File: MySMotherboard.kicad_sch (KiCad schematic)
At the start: 52 parts, among them SW1 RST, SW2 BTN, U1 MCP1640Cx-xCHY, U2 APE8865Y5-30-HF-3, U3 ATmega328PB-A, U4 AT25xxx, U5 RFM69HW, U6 ATSHA204A, U7 AP63205WU, U8 SP3481EN, X2 MySX 2.5, X3 ANT, Y1 16M

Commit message: add reverse polarity protection for 24V input
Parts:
- added Q2: ~, Package_TO_SOT_SMD:SOT-23, symbol Device:Q_PMOS_GSD
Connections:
- net +24V: now also Q2.2 (S); no longer X4.1 (Pin_1)
- net GND: now also Q2.1 (G)
- net SW_L2: no longer names the net of C6.2, L2.1, U7.5 (SW)
- new net: Q2.3 (D), X4.1 (Pin_1)
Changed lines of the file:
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@@
   (junction (at 57.15 78.105) (diameter 0) (color 0 0 0 0)
   )
+  (junction (at 254 121.285) (diameter 0) (color 0 0 0 0)
+  )
   (junction (at 63.5 31.115) (diameter 0) (color 0 0 0 0)
   )
@@
   (junction (at 82.55 90.17) (diameter 0) (color 0 0 0 0)
   )
-  (junction (at 271.78 130.81) (diameter 0) (color 0 0 0 0)
-  )
   (no_connect (at 180.975 144.78))
   (no_connect (at 180.975 139.7))
@@
     (stroke (width 0) (type default))
   )
+  (wire (pts (xy 264.16 121.285) (xy 271.78 121.285))
+    (stroke (width 0) (type default))
+  )
   (wire (pts (xy 72.39 121.285) (xy 111.125 121.285))
     (stroke (width 0.1524) (type solid))
@@
     (stroke (width 0.1524) (type solid))
   )
-  (wire (pts (xy 271.78 129.54) (xy 271.78 130.81))
-    (stroke (width 0) (type default))
-  )
   (wire (pts (xy 37.465 31.115) (xy 41.91 31.115))
     (stroke (width 0.1524) (type solid))
@@
     (stroke (width 0.1524) (type solid))
   )
-  (wire (pts (xy 271.78 130.81) (xy 271.78 134.62))
-    (stroke (width 0) (type default))
-  )
   (wire (pts (xy 195.58 41.275) (xy 200.025 41.275))
     (stroke (width 0.1524) (type solid))
@@
     (stroke (width 0) (type default))
   )
-  (wire (pts (xy 267.97 128.27) (xy 267.97 130.81))
-    (stroke (width 0) (type default))
-  )
   (wire (pts (xy 238.76 44.45) (xy 252.095 44.45))
     (stroke (width 0) (type default))
@@
     (stroke (width 0) (type default))
   )
+  (wire (pts (xy 251.46 121.285) (xy 254 121.285))
+    (stroke (width 0) (type default))
+  )
   (wire (pts (xy 182.245 41.275) (xy 195.58 41.275))
     (stroke (width 0.1524) (type solid))
@@
     (stroke (width 0.1524) (type solid))
   )
-  (wire (pts (xy 271.78 130.81) (xy 267.97 130.81))
-    (stroke (width 0) (type default))
-  )
   (wire (pts (xy 262.255 24.765) (xy 262.255 31.115))
     (stroke (width 0) (type default))
@@
     (stroke (width 0.1524) (type solid))
   )
+  (wire (pts (xy 271.78 121.285) (xy 271.78 134.62))
+    (stroke (width 0) (type default))
+  )
   (wire (pts (xy 55.88 31.115) (xy 63.5 31.115))
     (stroke (width 0) (type default))
@@
     (effects (font (size 1.27 1.27)) (justify left bottom))
   )
-  (label "SW_L2" (at 264.795 24.765 180) (fields_autoplaced)
-    (effects (font (size 1.27 1.27)) (justify right bottom))
-  )
   (label "A5" (at 78.105 121.285 0) (fields_autoplaced)
     (effects (font (size 1.2446 1.2446)) (justify left bottom))
@@
     )
   )
+  (netclass_flag "" (length 2.54) (shape round) (at 265.43 121.285 0) (fields_autoplaced)
+    (effects (font (size 1.27 1.27)) (justify left bottom))
+    (property "Netclass" "Power" (at 266.1285 118.745 0)
+      (effects (font (size 1.27 1.27) italic) (justify left))
+    )
+  )
+  (netclass_flag "" (length 2.54) (shape round) (at 262.255 24.765 0) (fields_autoplaced)
+    (effects (font (size 1.27 1.27)) (justify left bottom))
+    (property "Netclass" "Power" (at 261.5565 22.225 0)
+      (effects (font (size 1.27 1.27) italic) (justify right))
+    )
+  )
   (symbol (lib_id "power:GND") (at 88.9 81.28 0) (mirror x) (unit 1)
     (in_bom yes) (on_board yes) (dnp no) (fields_autoplaced)
@@
     )
   )
-  (symbol (lib_id "power:+24V") (at 267.97 128.27 0) (unit 1)
-    (in_bom yes) (on_board yes) (dnp no) (fields_autoplaced)
-    (property "Reference" "#PWR026" (at 267.97 132.08 0)
+  (symbol (lib_id "power:+24V") (at 254 121.285 0) (unit 1)
+    (in_bom yes) (on_board yes) (dnp no)
+    (property "Reference" "#PWR026" (at 254 125.095 0)
       (effects (font (size 1.27 1.27)) hide)
     )
-    (property "Value" "+24V" (at 267.97 123.19 0)
+    (property "Value" "+24V" (at 254 116.84 0)
       (effects (font (size 1.27 1.27)))
     )
-    (property "Footprint" "" (at 267.97 128.27 0)
+    (property "Footprint" "" (at 254 121.285 0)
       (effects (font (size 1.27 1.27)) hide)
     )
-    (property "Datasheet" "" (at 267.97 128.27 0)
+    (property "Datasheet" "" (at 254 121.285 0)
       (effects (font (size 1.27 1.27)) hide)
     )
@@
     )
   )
+  (symbol (lib_id "power:PWR_FLAG") (at 251.46 121.285 0) (mirror y) (unit 1)
+    (in_bom yes) (on_board yes) (dnp no)
+    (property "Reference" "#FLG04" (at 251.46 119.38 0)
+      (effects (font (size 1.27 1.27)) hide)
+    )
+    (property "Value" "PWR_FLAG" (at 250.825 117.475 0)
+      (effects (font (size 1.27 1.27)) (justify left))
+    )
+    (property "Footprint" "" (at 251.46 121.285 0)
+      (effects (font (size 1.27 1.27)) hide)
+    )
+    (property "Datasheet" "~" (at 251.46 121.285 0)
+      (effects (font (size 1.27 1.27)) hide)
+    )
+    (pin "1")
+    (instances
+      (project "MySMotherboard"
+        (path "/005ccf98-7ec2-4789-9497-178572c51999"
+          (reference "#FLG04") (unit 1)
+        )
+      )
+    )
+  )
   (symbol (lib_id "power:GND") (at 57.15 154.305 0) (unit 1)
     (in_bom yes) (on_board yes) (dnp no) (fields_autoplaced)
@@
     )
   )
-  (symbol (lib_id "power:PWR_FLAG") (at 271.78 129.54 0) (unit 1)
-    (in_bom yes) (on_board yes) (dnp no)
-    (property "Reference" "#FLG04" (at 271.78 127.635 0)
-      (effects (font (size 1.27 1.27)) hide)
-    )
-    (property "Value" "PWR_FLAG" (at 271.78 124.46 0)
-      (effects (font (size 1.27 1.27)) (justify left))
-    )
-    (property "Footprint" "" (at 271.78 129.54 0)
-      (effects (font (size 1.27 1.27)) hide)
-    )
-    (property "Datasheet" "~" (at 271.78 129.54 0)
-      (effects (font (size 1.27 1.27)) hide)
-    )
-    (pin "1")
-    (instances
-      (project "MySMotherboard"
-        (path "/005ccf98-7ec2-4789-9497-178572c51999"
-          (reference "#FLG04") (unit 1)
-        )
-      )
-    )
-  )
   (symbol (lib_id "Device:C") (at 58.42 47.625 0) (mirror y) (unit 1)
     (in_bom yes) (on_board yes) (dnp no)
@@
     )
   )
+  (symbol (lib_id "power:GND") (at 259.08 128.905 0) (unit 1)
+    (in_bom yes) (on_board yes) (dnp no) (fields_autoplaced)
+    (property "Reference" "#PWR025" (at 259.08 135.255 0)
+      (effects (font (size 1.27 1.27)) hide)
+    )
+    (property "Value" "GND" (at 259.08 133.35 0)
+      (effects (font (size 1.27 1.27)))
+    )
+    (property "Footprint" "" (at 259.08 128.905 0)
+      (effects (font (size 1.27 1.27)) hide)
+    )
+    (property "Datasheet" "" (at 259.08 128.905 0)
+      (effects (font (size 1.27 1.27)) hide)
+    )
+    (pin "1")
+    (instances
+      (project "MySMotherboard"
+        (path "/005ccf98-7ec2-4789-9497-178572c51999"
+          (reference "#PWR025") (unit 1)
+        )
+      )
+    )
+  )
   (symbol (lib_id "power:PWR_FLAG") (at 55.88 31.115 180) (unit 1)
     (in_bom yes) (on_board yes) (dnp no) (fields_autoplaced)
@@
         )
       )
+    )
+  )
+  (symbol (lib_id "Device:Q_PMOS_GSD") (at 259.08 123.825 270) (mirror x) (unit 1)
+    (in_bom yes) (on_board yes) (dnp no)
+    (property "Reference" "Q2" (at 259.08 116.84 90)
+      (effects (font (size 1.27 1.27)))
+    )
+    (property "Value" "~" (at 259.08 116.84 90)
+      (effects (font (size 1.27 1.27)))
+    )
+    (property "Footprint" "Package_TO_SOT_SMD:SOT-23" (at 261.62 118.745 0)
+      (effects (font (size 1.27 1.27)) hide)
+    )
+    (property "Datasheet" "~" (at 259.08 123.825 0)
+      (effects (font (size 1.27 1.27)) hide)
+    )
+    (pin "2")
+    (pin "1")
+    (pin "3")
+    (instances
+      (project "MySMotherboard"
+        (path "/005ccf98-7ec2-4789-9497-178572c51999"
+          (reference "Q2") (unit 1)
+        )
+      )

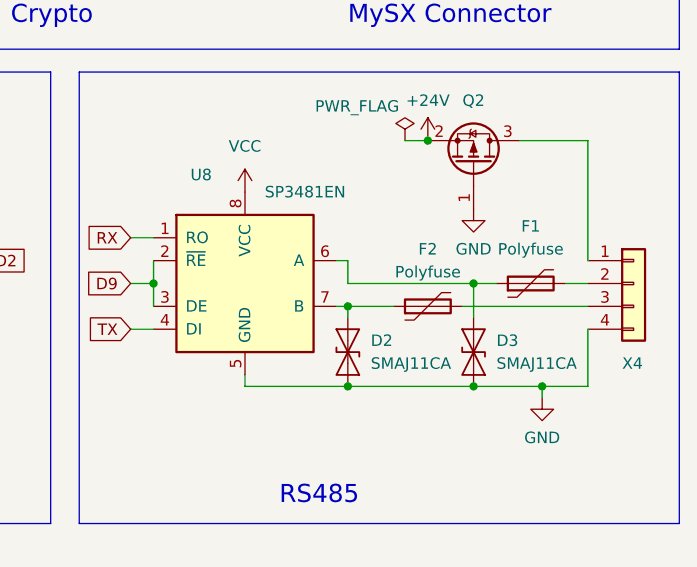
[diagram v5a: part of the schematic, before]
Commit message: update PCB with latest changes
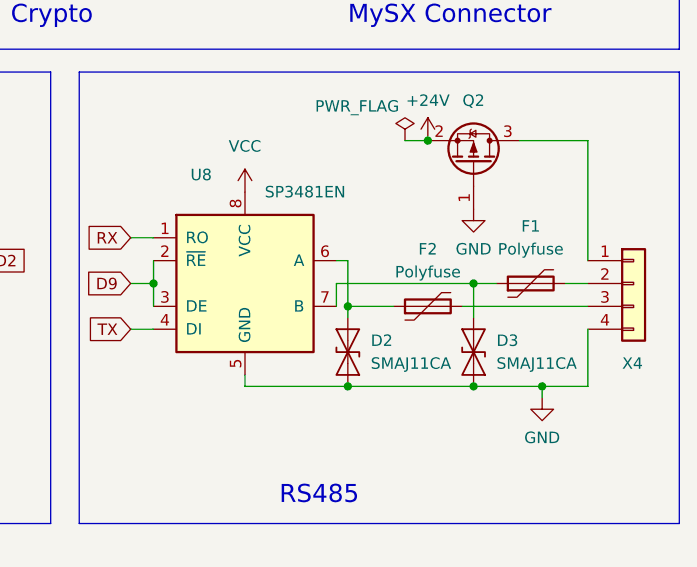
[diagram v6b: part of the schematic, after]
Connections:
- net at D3.2 (A2), F1.1: now also U8.7 (B); no longer U8.6 (A)
- net at D2.2 (A2), F2.1: now also U8.6 (A); no longer U8.7 (B)

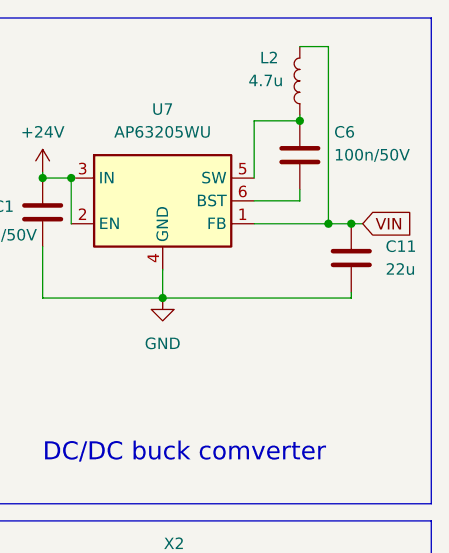
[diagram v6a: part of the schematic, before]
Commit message: change 22uF cap on buck converter output to 10uF
10uF should be sufficient
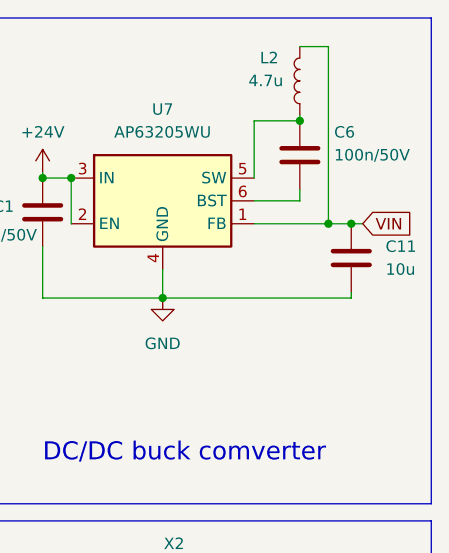
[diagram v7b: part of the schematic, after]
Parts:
- C11: value 22u -> 10u
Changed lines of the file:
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@@
       (effects (font (size 1.27 1.27)) (justify left))
     )
-    (property "Value" "22u" (at 276.86 41.275 0)
+    (property "Value" "10u" (at 276.86 41.275 0)
       (effects (font (size 1.27 1.27)) (justify left))
     )

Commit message: change bypass capacitor for buck converter from 0603 to 0402
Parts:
- C6: footprint Capacitor_SMD:C_0603_1608Metric_Pad1.08x0.95mm_HandSolder -> Capacitor_SMD:C_0402_1005Metric_Pad0.74x0.62mm_HandSolder
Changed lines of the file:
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@@
       (effects (font (size 1.27 1.27)) (justify left))
     )
-    (property "Footprint" "Capacitor_SMD:C_0603_1608Metric_Pad1.08x0.95mm_HandSolder" (at 268.3002 24.765 0)
+    (property "Footprint" "Capacitor_SMD:C_0402_1005Metric_Pad0.74x0.62mm_HandSolder" (at 268.3002 24.765 0)
       (effects (font (size 1.27 1.27)) hide)
     )
